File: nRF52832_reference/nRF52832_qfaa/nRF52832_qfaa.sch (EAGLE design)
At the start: 16 parts, among them U1 NRF52832, X1 32MHz, X2 32.768kHz

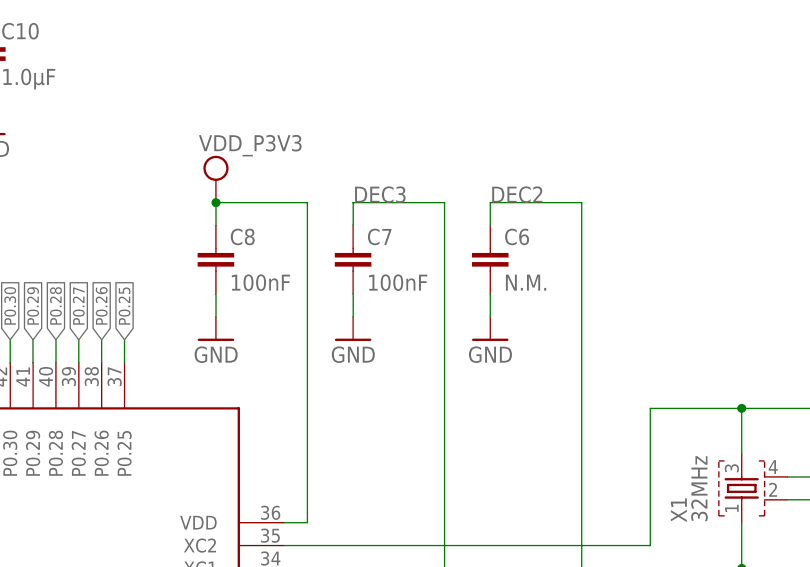
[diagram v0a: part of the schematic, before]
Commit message: Issue #2: Fixed value of C7 from 100nF to 100pF
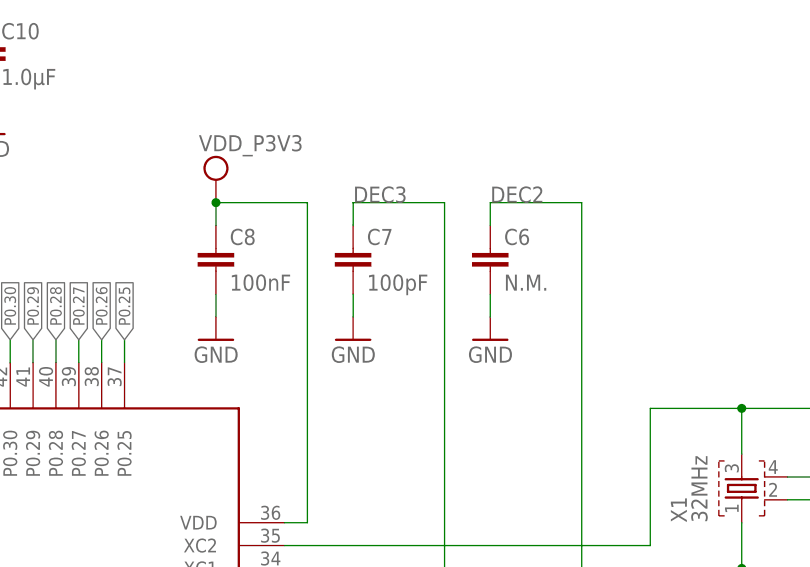
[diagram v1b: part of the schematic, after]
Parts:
- C7: value 100nF -> 100pF
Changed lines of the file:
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@@
 <part name="C5" library="Nordic_nRF" deviceset="CAPACITOR" device="_0402_N" value="100nF"/>
 <part name="C6" library="Nordic_nRF" deviceset="CAPACITOR" device="_0402_N" value="N.M."/>
-<part name="C7" library="Nordic_nRF" deviceset="CAPACITOR" device="_0402_N" value="100nF"/>
+<part name="C7" library="Nordic_nRF" deviceset="CAPACITOR" device="_0402_N" value="100pF"/>
 <part name="C8" library="Nordic_nRF" deviceset="CAPACITOR" device="_0402_N" value="100nF"/>
 <part name="C9" library="Nordic_nRF" deviceset="CAPACITOR" device="_0603_N" value="4.7µF"/>

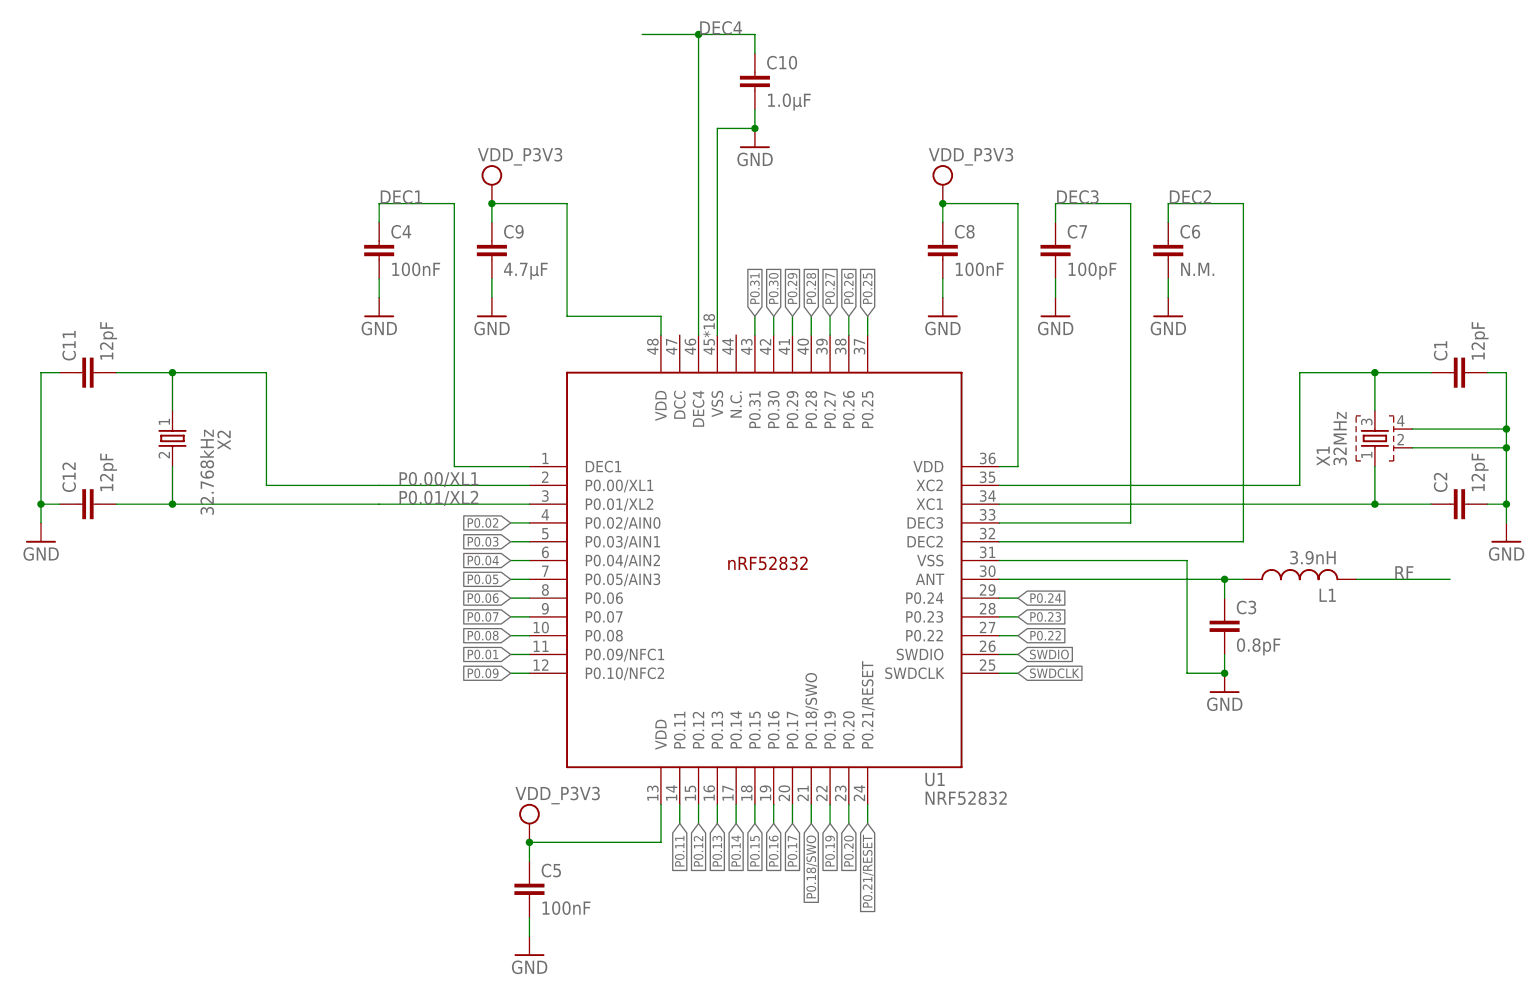
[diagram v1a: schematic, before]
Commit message: Same fixes as in qfaa_dcdc
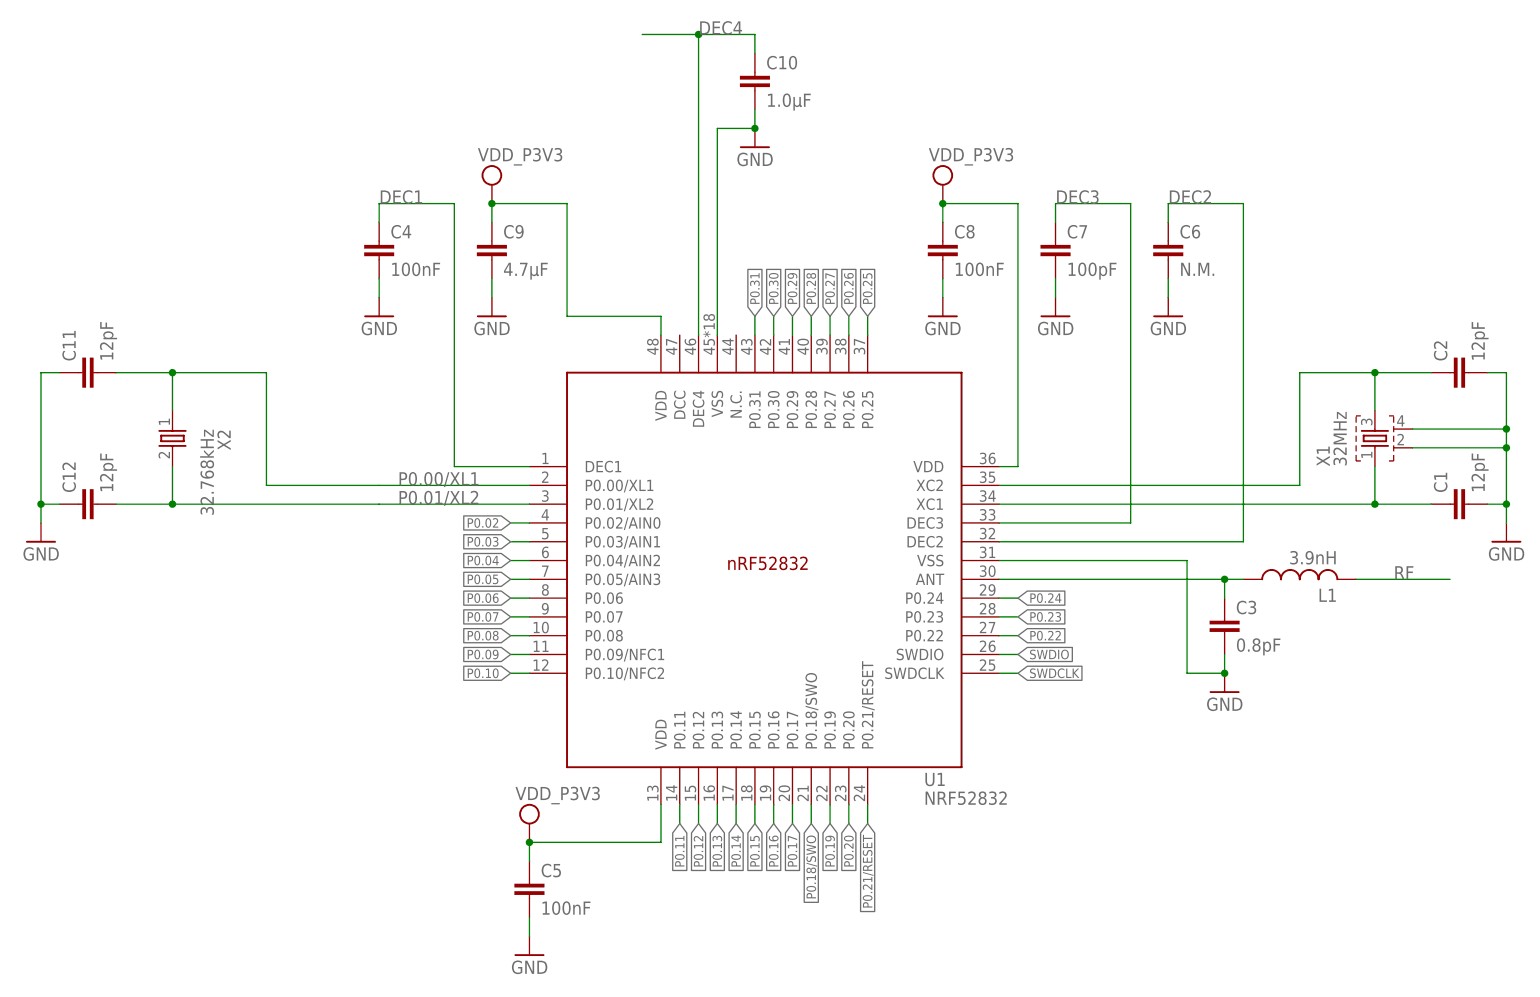
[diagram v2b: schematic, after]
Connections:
- removed net P0.01: U1.P0.09/NFC1@11
- new net P0.10: U1.P0.10/NFC2@12
- net N$3: now also C2.1; no longer C1.1
- net P0.09: now also U1.P0.09/NFC1@11; no longer U1.P0.10/NFC2@12
- net X1: now also C1.1; no longer C2.1
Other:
- moved on the sheet: C1, C2
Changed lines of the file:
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@@
 <?xml version="1.0" encoding="utf-8"?>
 <!DOCTYPE eagle SYSTEM "eagle.dtd">
-<eagle version="7.6.0">
+<eagle version="8.3.0">
 <drawing>
 <settings>
 <setting alwaysvectorfont="no"/>
+<setting keepoldvectorfont="yes"/>
 <setting verticaltext="up"/>
 </settings>
@@
 <part name="X2" library="Nordic_nRF" deviceset="XTAL_32KHZ" device="" value="32.768kHz"/>
 <part name="L1" library="Nordic_nRF" deviceset="INDUCTOR" device="_0402_N" value="3.9nH"/>
+<part name="C2" library="Nordic_nRF" deviceset="CAPACITOR" device="_0402_N" value="12pF"/>
 <part name="C1" library="Nordic_nRF" deviceset="CAPACITOR" device="_0402_N" value="12pF"/>
-<part name="C2" library="Nordic_nRF" deviceset="CAPACITOR" device="_0402_N" value="12pF"/>
 <part name="C3" library="Nordic_nRF" deviceset="CAPACITOR" device="_0402_N" value="0.8pF"/>
 <part name="C4" library="Nordic_nRF" deviceset="CAPACITOR" device="_0402_N" value="100nF"/>
@@
 <instance part="X1" gate="X$1" x="205.74" y="101.6" rot="R90"/>
 <instance part="L1" gate="L$1" x="193.04" y="86.36" rot="R90"/>
-<instance part="C1" gate="C$1" x="213.36" y="114.3" rot="R90"/>
-<instance part="C2" gate="C$1" x="213.36" y="96.52" rot="R90"/>
+<instance part="C2" gate="C$1" x="213.36" y="114.3" rot="R90"/>
+<instance part="C1" gate="C$1" x="213.36" y="96.52" rot="R90"/>
 <instance part="C3" gate="C$1" x="182.88" y="81.28"/>
 <instance part="C4" gate="C$1" x="68.58" y="132.08"/>
@@
 <pinref part="X1" gate="X$1" pin="4"/>
 <pinref part="X1" gate="X$1" pin="2"/>
+<pinref part="C2" gate="C$1" pin="2"/>
 <pinref part="C1" gate="C$1" pin="2"/>
-<pinref part="C2" gate="C$1" pin="2"/>
 </segment>
 <segment>
@@
 <wire x1="193.04" y1="99.06" x2="152.4" y2="99.06" width="0.1524" layer="91"/>
 <pinref part="X1" gate="X$1" pin="3"/>
-<pinref part="C1" gate="C$1" pin="1"/>
+<pinref part="C2" gate="C$1" pin="1"/>
 </segment>
 </net>
@@
 <junction x="203.2" y="96.52"/>
 <pinref part="X1" gate="X$1" pin="1"/>
-<pinref part="C2" gate="C$1" pin="1"/>
+<pinref part="C1" gate="C$1" pin="1"/>
 </segment>
 </net>
@@
 </segment>
 </net>
-<net name="P0.09" class="0">
+<net name="P0.10" class="0">
 <segment>
 <label x="86.36" y="73.66" size="1.27" layer="95" rot="R180" xref="yes"/>
@@
 </segment>
 </net>
-<net name="P0.01" class="0">
+<net name="P0.09" class="0">
 <segment>
 <wire x1="86.36" y1="76.2" x2="88.9" y2="76.2" width="0.1524" layer="91"/>
